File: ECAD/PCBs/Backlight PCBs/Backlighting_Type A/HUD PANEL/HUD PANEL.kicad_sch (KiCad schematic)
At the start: 74 parts, among them J1 Molex 2x02 Mini-Fit Jr., J2 Molex 2x02 Mini-Fit Jr.

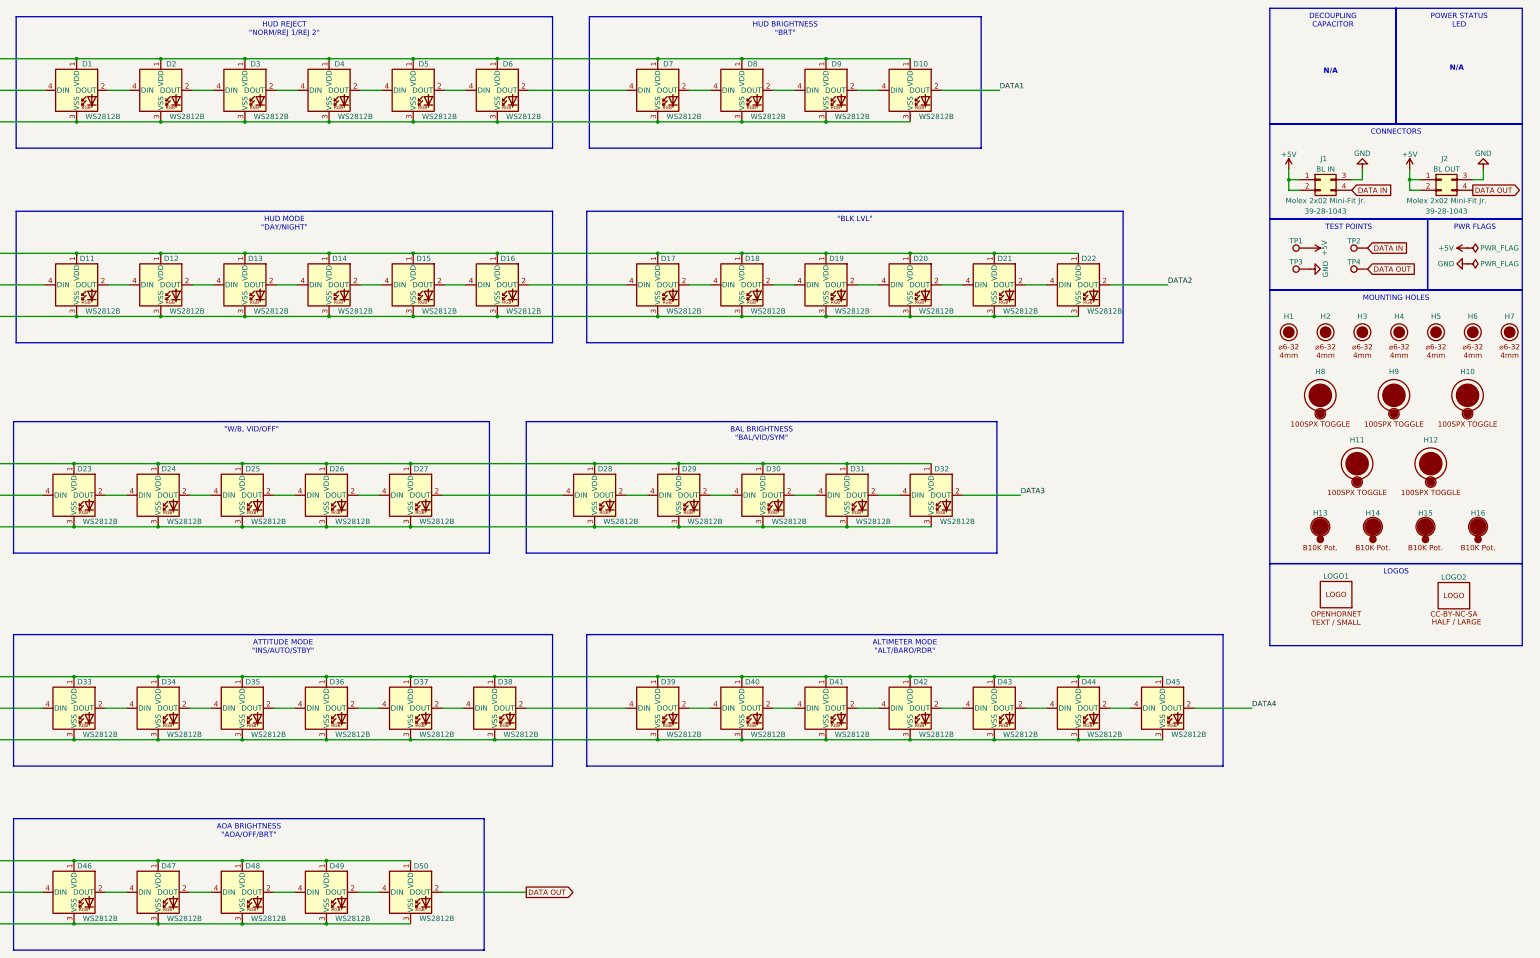
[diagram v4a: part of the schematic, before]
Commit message: KiCad 7 Transition - HUD Panel
PCB & Schematic standardization
Updated Footprint Metadata
Updated Silkscreen text
Recompiled Assets and Manufacturing Files
Removed DXF file used to assist in LED placement
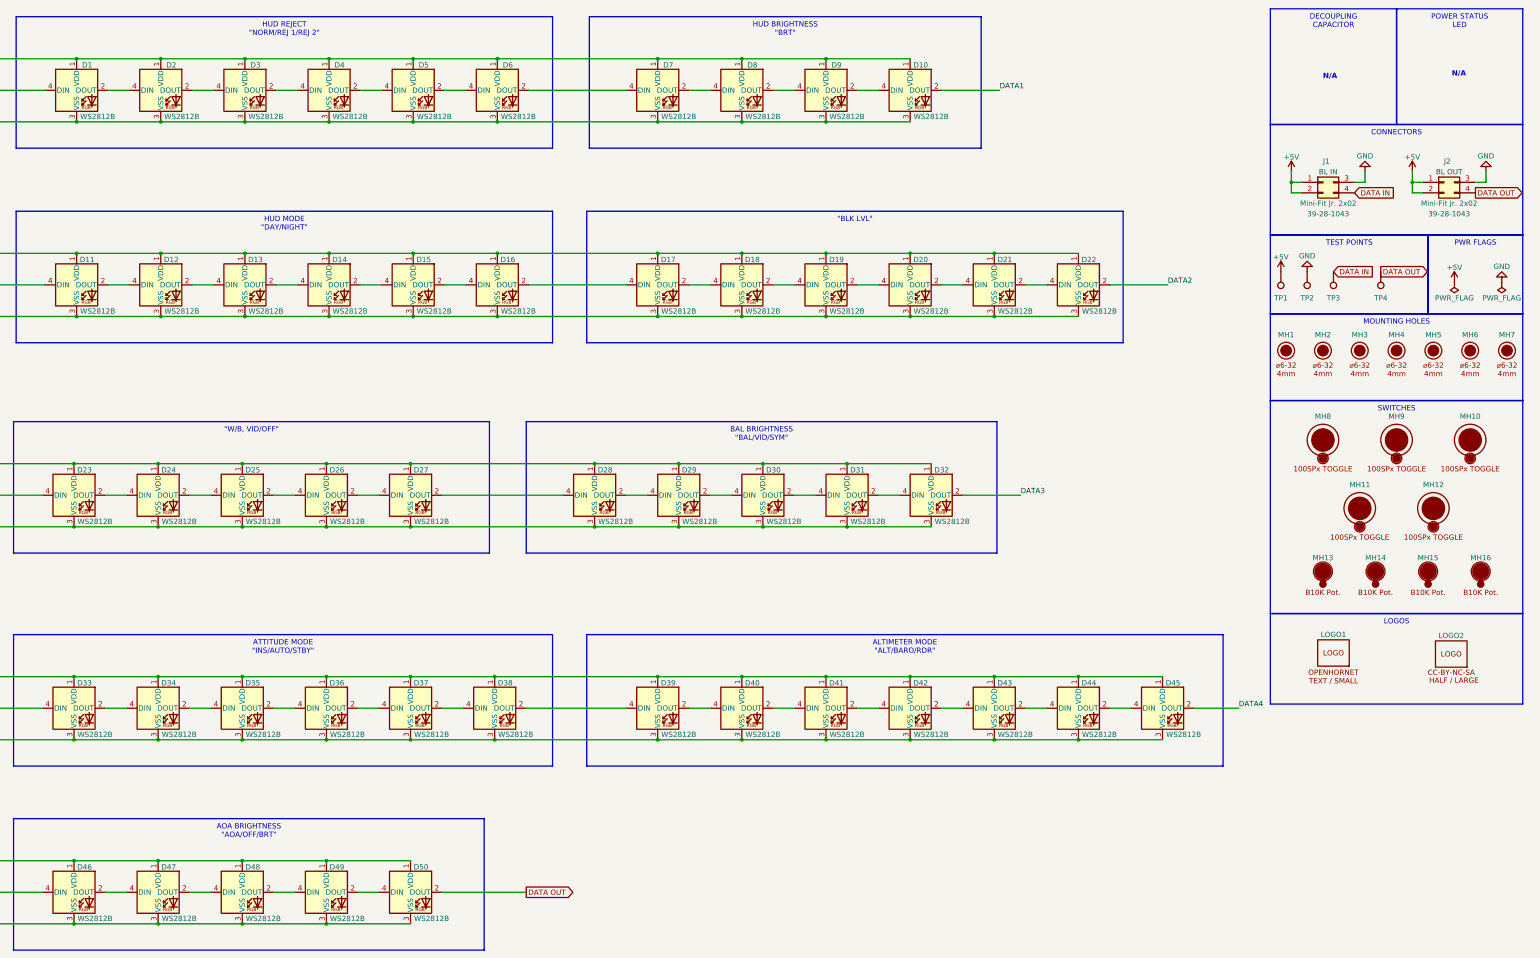
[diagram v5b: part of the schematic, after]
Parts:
- D1, D10, D11, D12, D13, D14, D15, D16, D17, D18, D19, D2, D20, D21, D22, D23, D24, D25, D26, D27, D28, D29, D3, D30, D31, D32, D33, D34, D35, D36, D37, D38, D39, D4, D40, D41, D42, D43, D44, D45, D46, D47, D48, D49, D5, D50, D6, D7, D8, D9: value RGB -> WS2812B
- J1, J2: value Molex 2x02 Mini-Fit Jr. -> Mini-Fit Jr. 2x02; symbol OH_Symbols:Molex_2x02_Mini-Fit_Jr. -> OH_Symbols:Molex_Mini-Fit_Jr._2x02
- LOGO2: now left out of the parts list
- MH1: renamed from H1; value #6-32/4mm -> 6x32 / 4mm
- MH10: renamed from H10; value 12.7mm -> Switch_100SPx; symbol OH_Symbols:MountingHole_100SPX_Toggle -> OH_Symbols:MountingHole_100SPx_Toggle
- MH11: renamed from H11; value 12.7mm -> Switch_100SPx; symbol OH_Symbols:MountingHole_100SPX_Toggle -> OH_Symbols:MountingHole_100SPx_Toggle
- MH12: renamed from H12; value 12.7mm -> Switch_100SPx; symbol OH_Symbols:MountingHole_100SPX_Toggle -> OH_Symbols:MountingHole_100SPx_Toggle
- MH13: renamed from H13; value 11mm -> Pot_B10K; Manufacturer PN (none) -> P0915N-FC20BR10K
- MH14: renamed from H14; value 11mm -> Pot_B10K; Manufacturer PN (none) -> P0915N-FC20BR10K
- MH15: renamed from H15; value 11mm -> Pot_B10K; Manufacturer PN (none) -> P0915N-FC20BR10K
- MH16: renamed from H16; value 11mm -> Pot_B10K; Manufacturer PN (none) -> P0915N-FC20BR10K
- MH2: renamed from H2; value #6-32/4mm -> 6x32 / 4mm
- MH3: renamed from H3; value #6-32/4mm -> 6x32 / 4mm
- MH4: renamed from H4; value #6-32/4mm -> 6x32 / 4mm
- MH5: renamed from H5; value #6-32/4mm -> 6x32 / 4mm
- MH6: renamed from H6; value #6-32/4mm -> 6x32 / 4mm
- MH7: renamed from H7; value #6-32/4mm -> 6x32 / 4mm
- MH8: renamed from H8; value 12.7mm -> Switch_100SPx; symbol OH_Symbols:MountingHole_100SPX_Toggle -> OH_Symbols:MountingHole_100SPx_Toggle
- MH9: renamed from H9; value 12.7mm -> Switch_100SPx; symbol OH_Symbols:MountingHole_100SPX_Toggle -> OH_Symbols:MountingHole_100SPx_Toggle
- TP1: Silkscreen (none) -> TP1; now left out of the parts list
- TP2: Silkscreen (none) -> TP2; now left out of the parts list
- TP3: Silkscreen (none) -> TP3; now left out of the parts list
- TP4: Silkscreen (none) -> TP4; now left out of the parts list
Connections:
- net DATA IN: now also TP3.1; no longer TP2.1
- net GND: now also TP2.1; no longer TP3.1
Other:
- company: WWW.OPENHORNET.COM -> www.openhornet.com
- moved on the sheet: J1, J2, LOGO1, LOGO2, MH1, MH10, MH11, MH12, MH13, MH14, MH15, MH16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
